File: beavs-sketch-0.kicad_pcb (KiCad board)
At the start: 4 copper layers, 50 x 70 mm, 80 parts, among them J1 USB_C_Receptacle_USB2.0_16P, J10 Conn_01x03, J11 Conn_01x03, J12 Micro_SD_Card, J2 Conn_Coaxial, J3 Conn_01x02, J4 Conn_Coaxial, J5 Conn_01x02, J6 Conn_01x03, J7 Conn_01x03, J8 Conn_01x03, J9 Conn_01x03, Q2 SiS427EDN, U1 RP2040, U10 INA745A, U11 INA745A, U12 INA745A, U13 INA745A, U14 ISM6HG256X, U15 SN74LVC8T245, U16 SRV05-4, U2 W25Q128JVS, U3 MS5607-02BA, U4 RFM95W-915S2, U5 MAX-M10S, U6 INA745A, U7 AMS1117-3.3, U8 AMS1117-5.0, U9 INA745A, Y1 Crystal_GND24

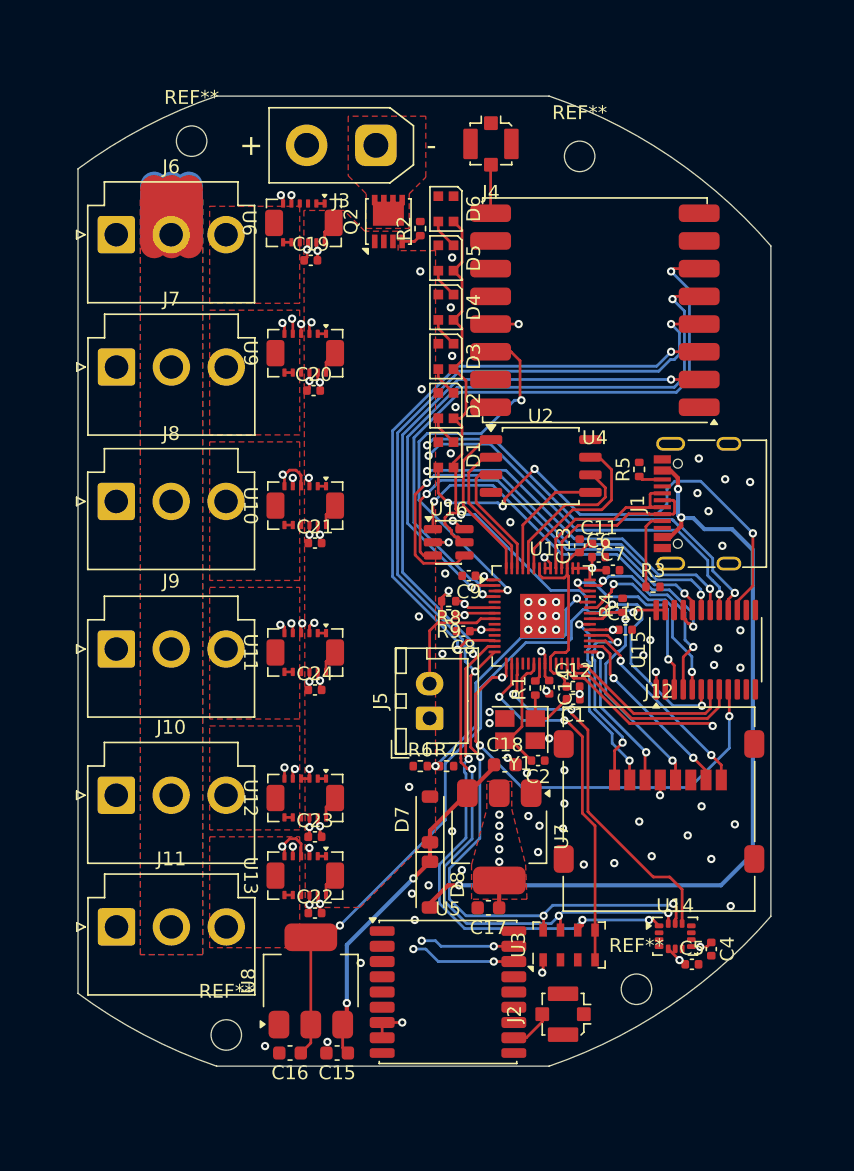
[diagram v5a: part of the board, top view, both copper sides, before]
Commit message: update schematics and add 3d models
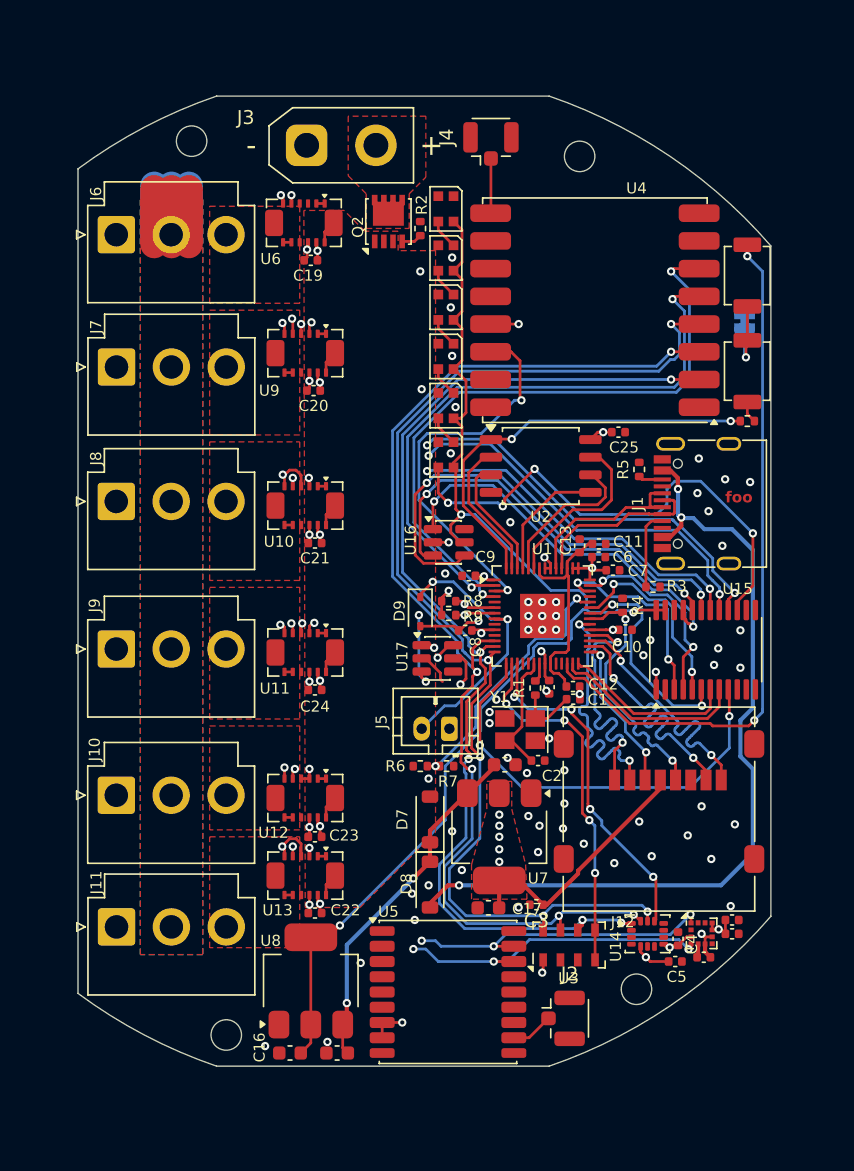
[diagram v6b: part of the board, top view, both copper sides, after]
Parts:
- added C25: 100n, Capacitor_SMD:C_0402_1005Metric, F.Cu at (216.0, 77.3)
- added C26: 100n, Capacitor_SMD:C_0402_1005Metric, F.Cu at (224.2, 113.5)
- added C28: 10u, Capacitor_SMD:C_0402_1005Metric, F.Cu at (224.2, 112.5)
- added C29: 220n, Capacitor_SMD:C_0402_1005Metric, F.Cu at (222.2, 115.2)
- added C3: 10u, Capacitor_SMD:C_0402_1005Metric, F.Cu at (210.1, 111.4)
- added D9: D_Zener, Diode_SMD:D_SOD-323, F.Cu at (201.7, 90.2)
- added JP1: SolderJumper_2_Bridged, Jumper:SolderJumper-2_P1.3mm_Bridged_RoundedPad1.0x1.5mm, B.Cu at (225.1, 69.3)
- added R10: 1k, Resistor_SMD:R_0402_1005Metric, F.Cu at (225.3, 76.5)
- added SW1: SW_Push, beavs-footprints:SW_SPST_TS-1088-AR02016, F.Cu at (225.3, 66.0)
- added SW2: SW_Push, beavs-footprints:SW_SPST_TS-1088-AR02016, F.Cu at (225.3, 72.9)
- added U17: SRV05-4, Package_TO_SOT_SMD:SOT-23-6, F.Cu at (202.9, 93.6)
- added U18: LIS2MDL, Package_LGA:LGA-12_2x2mm_P0.5mm, F.Cu at (222.0, 113.5)
- J2, J4: footprint Connector_Coaxial:U.FL_Molex_MCRF_73412-0110_Vertical -> Connector_Coaxial:U.FL_Hirose_U.FL-R-SMT-1_Vertical
- J3: footprint Connector_AMASS:AMASS_XT30UPB-F_1x02_P5.0mm_Vertical -> Connector_AMASS:AMASS_XT30UPB-M_1x02_P5.0mm_Vertical
- J5: footprint Connector_JST:JST_XH_B2B-XH-A_1x02_P2.50mm_Vertical -> Connector_JST:JST_PH_B2B-PH-K_1x02_P2.00mm_Vertical
- moved J3 5.00 mm to (193.5, 56.6), turned to 0 degrees
- moved C4 2.51 mm to (220.3, 113.9), turned to 90 degrees
- moved U14 2.00 mm to (218.1, 113.5)
- moved J5 1.61 mm to (203.8, 98.7), turned to 180 degrees
- moved C5 1.22 mm to (220.1, 115.5)
- moved J2 0.30 mm to (212.0, 119.6), turned to 0 degrees
- moved C8 0.15 mm to (204.9, 91.6)
- turned J4 to 90 degrees
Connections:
- J3 pad 1: Net-(J3-Pin_1) -> GND
- J3 pad 2: GND -> Net-(J3-Pin_2)
- Q2 pad 5: Net-(J3-Pin_1) -> Net-(J3-Pin_2)
- U16 pad 6: /servos/S4 -> unconnected-(U16-IO4-Pad6)
- U2 pad 8: unconnected-(U2-VCC-Pad8) -> +3V3
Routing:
- net /mcu/~{RESET}: track 12.7 -> 50.9 mm, vias 1 -> 2
- net +3V3: track 40.6 -> 62.1 mm, vias 29 -> 30
- net Net-(U1-QSPI_SS): track 11.7 -> 30.2 mm, vias 0 -> 2
- net /Sensors/SCL: track 95.8 -> 112.4 mm, vias 9 -> 10
- net /Sensors/SDA: track 92.5 -> 108.6 mm, vias 9 -> 10
- net /ARM_SWITCH: track 8.87 -> 19.9 mm, vias 0 -> 2
- net GND: track 12.2 -> 22.1 mm, vias 68 -> 70
- net /servos/S5: track 75.4 -> 83.7 mm, vias 3 -> 4
- net Net-(JP1-B): track 0.00 -> 5.71 mm, vias 0 -> 1
- net /SD Card/DAT0: track 13.7 -> 18.4 mm
- net /SD Card/DAT3: track 13.6 -> 18.3 mm
- net +5V: track 89.9 -> 94.6 mm, vias 3 -> 5
- net /SD Card/DAT1: track 14.6 -> 18.4 mm
- net /servos/S6: track 86.3 -> 89.8 mm, vias 3 -> 4
- net /SD Card/DAT2: track 14.9 -> 18.4 mm
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- added copper zone on F.Cu, net Net-(J3-Pin_2)
- removed copper zone on F.Cu, net Net-(J3-Pin_1)
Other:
- board text added: "foo"

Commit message: cleanup
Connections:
- U15 pad 10: unconnected-(U15-A8-Pad10) -> GND
- U15 pad 2: unconnected-(U15-DIR-Pad2) -> +3V3
- U15 pad 22: unconnected-(U15-~{OE}-Pad22) -> GND
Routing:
- net +5V: track 94.6 -> 88.3 mm
- net Net-(U1-QSPI_SD2): track 8.90 -> 12.9 mm
- net Net-(U1-QSPI_SD0): track 8.99 -> 12.9 mm
- net Net-(U1-QSPI_SD1): track 10.3 -> 13.0 mm
- net Net-(U1-QSPI_SCLK): track 10.9 -> 13.0 mm
- net GND: vias 70 -> 69
- added copper zone on F.Cu, net +5V

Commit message: change out LEDs, add silk, start getting ready for fab
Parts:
- added D10: LED, LED_SMD:LED_0805_2012Metric, F.Cu at (200.5, 110.7)
- added R11: 10, Resistor_SMD:R_0402_1005Metric, F.Cu at (199.0, 111.3)
- added REF**: ToolingHole_1.152mm, MountingHole:ToolingHole_1.152mm, F.Cu at (183.7, 119.6)
- added REF**: ToolingHole_1.152mm, MountingHole:ToolingHole_1.152mm, F.Cu at (210.5, 54.5)
- added REF**: ToolingHole_1.152mm, MountingHole:ToolingHole_1.152mm, F.Cu at (180.6, 57.8)
- added REF**: ToolingHole_1.152mm, MountingHole:ToolingHole_1.152mm, F.Cu at (214.0, 117.1)
- added REF**: aiaa-mask-silk-8x4, beavs-footprints:aiaa-mask-silk-8x4, F.Cu at (196.2, 88.1)
- D1, D2, D3, D4, D5, D6: value WS2812B-2020 -> SK6812-EC20; footprint LED_SMD:LED_WS2812B-2020_PLCC4_2.0x2.0mm -> beavs-footprints:LED_SK6812-EC20_PLCC4_2.0x2.0mm
- JP1: moved to F.Cu
- moved JP1 12.9 mm to (217.7, 58.7), turned to 0 degrees
- moved J8 0.73 mm to (179.8, 83.0)
- moved R2 0.73 mm to (201.3, 62.0)
- moved Q2 0.64 mm to (199.0, 61.6)
- moved J10 0.49 mm to (179.8, 103.0)
- moved J7 0.44 mm to (179.8, 73.0)
- moved J3 0.30 mm to (193.5, 56.3)
- moved J2 0.21 mm to (212.2, 119.5), turned to 45 degrees
- moved D7 0.20 mm to (202.6, 105.2)
- moved D8 0.20 mm to (202.6, 110.0)
- moved R10 0.10 mm to (225.4, 76.5)
- moved J9 0.07 mm to (179.8, 93.0)
- turned D1 to 90 degrees
- turned D2 to 90 degrees
- turned D3 to 90 degrees
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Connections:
- D1 pad 1: Net-(D1-DOUT) -> +5V
- D1 pad 2: GND -> Net-(D1-DOUT)
- D1 pad 3: Net-(D1-DIN) -> GND
- D1 pad 4: +5V -> Net-(D1-DIN)
- D2 pad 1: Net-(D2-DOUT) -> +5V
- D2 pad 2: GND -> Net-(D2-DOUT)
- D2 pad 3: Net-(D1-DOUT) -> GND
- D2 pad 4: +5V -> Net-(D1-DOUT)
- D3 pad 1: Net-(D3-DOUT) -> +5V
- D3 pad 2: GND -> Net-(D3-DOUT)
- D3 pad 3: Net-(D2-DOUT) -> GND
- D3 pad 4: +5V -> Net-(D2-DOUT)
- D4 pad 1: Net-(D4-DOUT) -> +5V
- D4 pad 2: GND -> Net-(D4-DOUT)
- D4 pad 3: Net-(D3-DOUT) -> GND
- D4 pad 4: +5V -> Net-(D3-DOUT)
- D5 pad 1: Net-(D5-DOUT) -> +5V
- D5 pad 2: GND -> Net-(D5-DOUT)
- D5 pad 3: Net-(D4-DOUT) -> GND
- D5 pad 4: +5V -> Net-(D4-DOUT)
- D6 pad 1: unconnected-(D6-DOUT-Pad1) -> +5V
- D6 pad 2: GND -> unconnected-(D6-DOUT-Pad2)
- D6 pad 3: Net-(D5-DOUT) -> GND
- D6 pad 4: +5V -> Net-(D5-DOUT)
- U1 pad 39: unconnected-(U1-GPIO27_ADC1-Pad39) -> /Sensors/EXTINT
- U5 pad 4: unconnected-(U5-TIMEPULSE-Pad4) -> Net-(U5-TIMEPULSE)
- U5 pad 5: unconnected-(U5-EXTINT-Pad5) -> /Sensors/EXTINT
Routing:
- net /Sensors/EXTINT: track 0.00 -> 38.2 mm, vias 0 -> 3
- net Net-(JP1-B): track 5.71 -> 14.9 mm, vias 1 -> 2
- net GND: track 22.1 -> 31.0 mm, vias 69 -> 104
- net Net-(U5-TIMEPULSE): track 0.00 -> 6.29 mm
- net VBUS: track 60.5 -> 57.1 mm
- net Net-(U1-QSPI_SS): track 30.1 -> 33.2 mm
- net +5V: track 88.3 -> 91.0 mm, vias 5 -> 6
- net Net-(D10-A): track 0.00 -> 1.86 mm
- net /servos/S5: track 83.7 -> 82.4 mm
- net /servos/S3: track 58.8 -> 57.8 mm
- net /mcu/M_LED_D: track 31.4 -> 32.3 mm
- net Net-(D1-DIN): track 36.8 -> 36.1 mm
- net +3V3: track 62.1 -> 62.8 mm
- net Net-(D4-DOUT): track 2.18 -> 2.75 mm
- net Net-(D3-DOUT): track 2.18 -> 2.75 mm
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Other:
- board text added: "ASDT"
- board text added: "B"
- board text added: "Baro"
- board text added: "IMU"
- board text added: "Mag"
- board text added: "R"
- board text added: "Radio"
- board text added: "SCRT"
- board text added: "SD"
- board text added: "Status"
